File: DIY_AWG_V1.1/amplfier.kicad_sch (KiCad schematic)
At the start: 22 parts, among them IC3 LMH6505MAX, IC4 THS3091DDAR

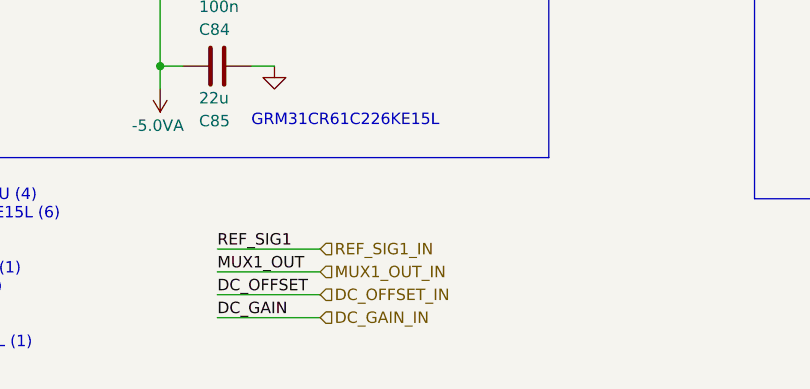
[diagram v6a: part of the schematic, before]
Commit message: Updated schematics to clear ERCs
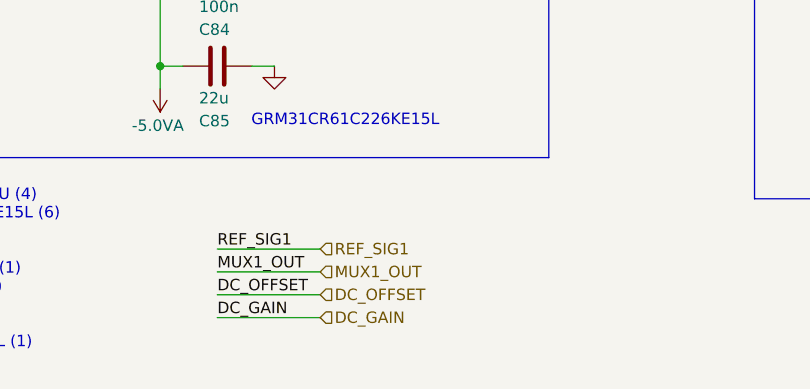
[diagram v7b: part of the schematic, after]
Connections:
- net DC_GAIN_IN renamed DC_GAIN
- net DC_OFFSET_IN renamed DC_OFFSET
- net MUX1_OUT_IN renamed MUX1_OUT
- net REF_SIG1_IN renamed REF_SIG1
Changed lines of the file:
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@@
 		)
 	)
-	(hierarchical_label "REF_SIG1_IN"
+	(hierarchical_label "REF_SIG1"
 		(shape input)
 		(at 86.36 85.09 0)
@@
 		)
 	)
-	(hierarchical_label "MUX1_OUT_IN"
+	(hierarchical_label "MUX1_OUT"
 		(shape input)
 		(at 86.36 87.63 0)
@@
 		)
 	)
-	(hierarchical_label "DC_OFFSET_IN"
+	(hierarchical_label "DC_OFFSET"
 		(shape input)
 		(at 86.36 90.17 0)
@@
 		)
 	)
-	(hierarchical_label "DC_GAIN_IN"
+	(hierarchical_label "DC_GAIN"
 		(shape input)
 		(at 86.36 92.71 0)

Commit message: Updated the schematics to resolve ERCs
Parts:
- IC3: footprint SOIC127P600X175-8N -> easyeda2kicad:SOP-8_L4.9-W3.9-P1.27-LS6.0-BL
- IC4: footprint SOIC127P600X170-9N -> easyeda2kicad:SOIC-8_L4.9-W3.9-P1.27-LS6.0-BL-EP
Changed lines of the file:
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@@
 			)
 		)
-		(property "Footprint" "SOIC127P600X175-8N"
+		(property "Footprint" "easyeda2kicad:SOP-8_L4.9-W3.9-P1.27-LS6.0-BL"
 			(at 60.96 138.1 0)
 			(hide yes)
@@
 			)
 		)
-		(property "Footprint" "SOIC127P600X170-9N"
+		(property "Footprint" "easyeda2kicad:SOIC-8_L4.9-W3.9-P1.27-LS6.0-BL-EP"
 			(at 199.39 143.18 0)
 			(hide yes)
